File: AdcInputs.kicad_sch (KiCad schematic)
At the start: 38 parts, among them U31 AMC1100DWV, U32 AMC1100DWV, U33 AMC1100DWV, U34 AMC1100DWV, U6 CD4051B, U7 CD4051B, U8 CD4052B, U9 LTV-247

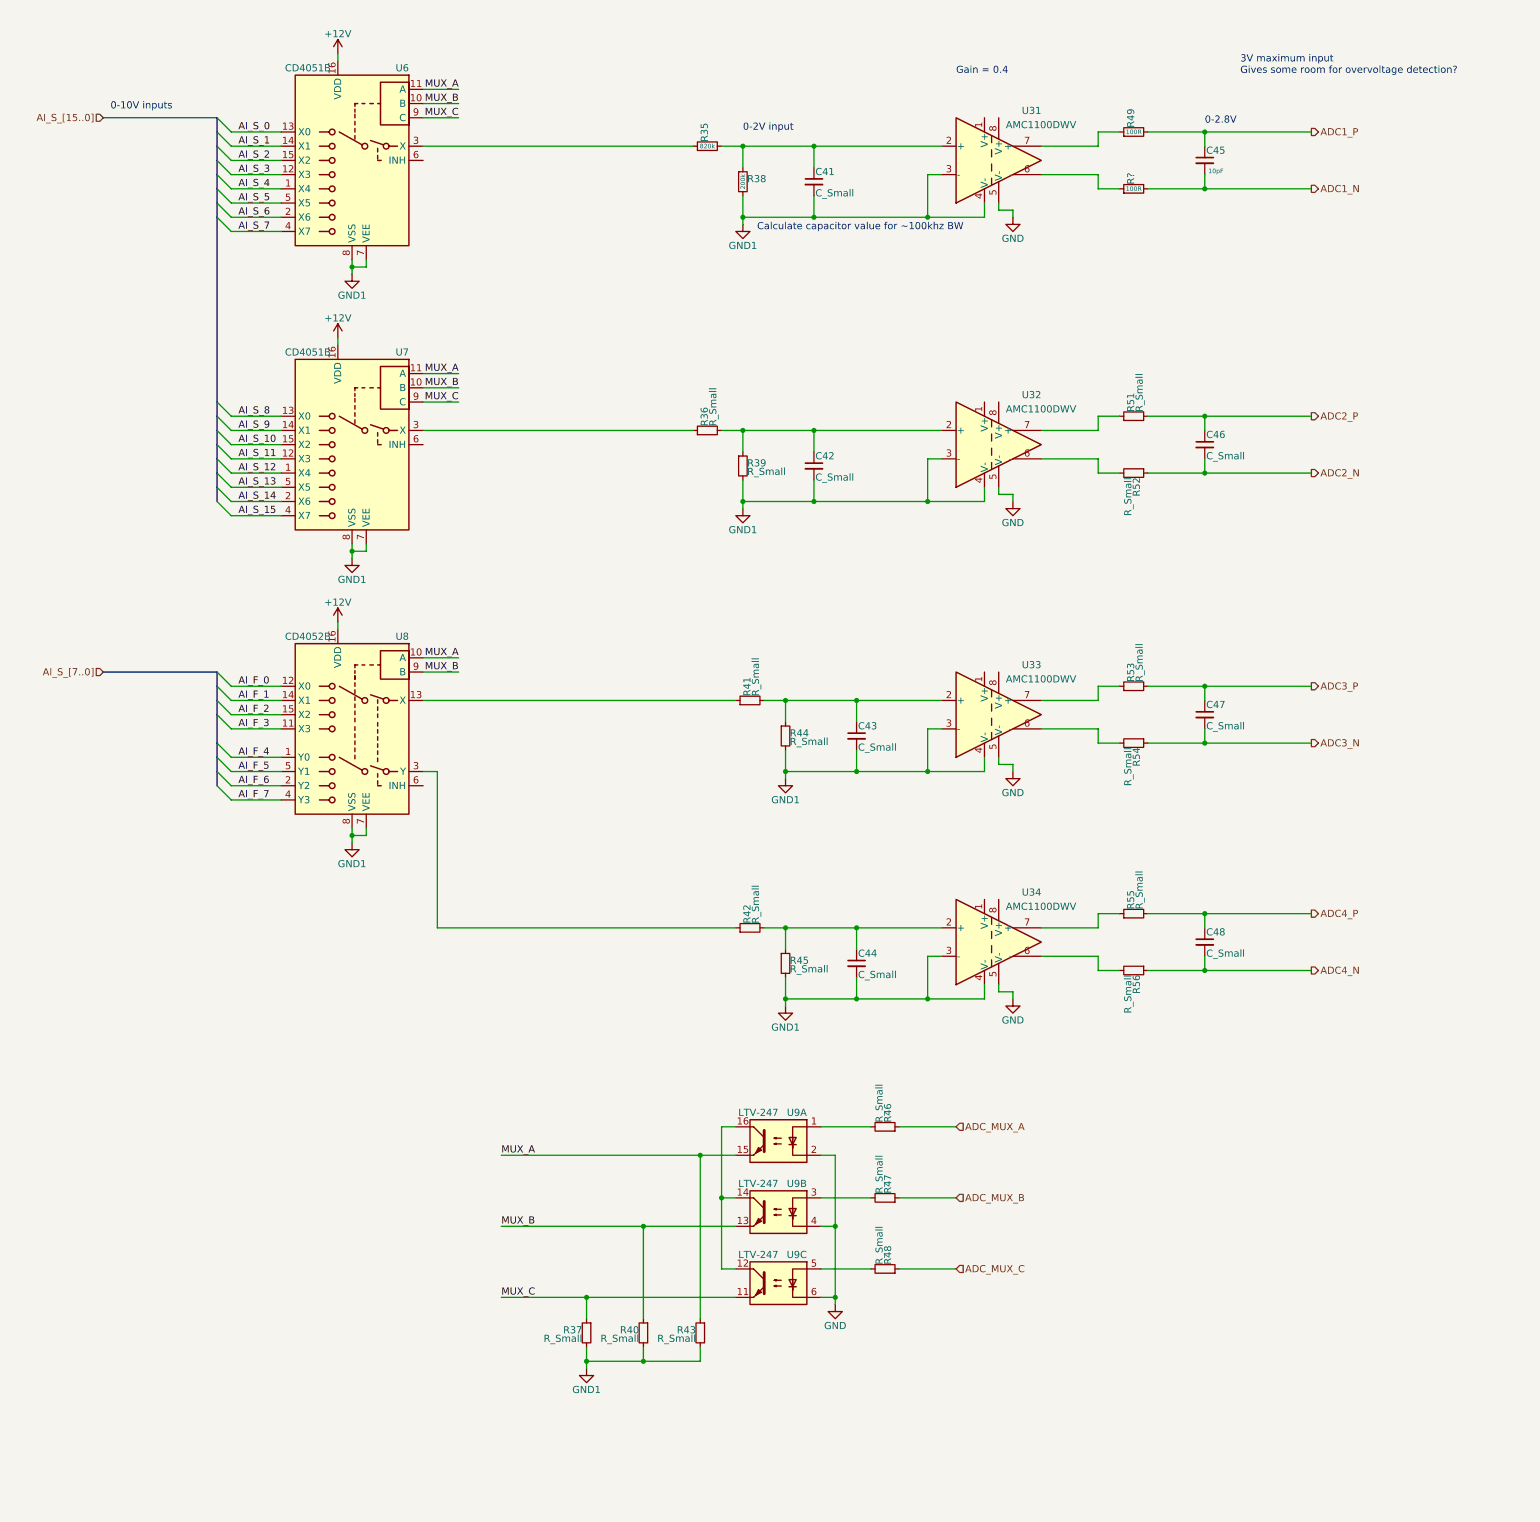
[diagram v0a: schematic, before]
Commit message: analog inputs, timer IO
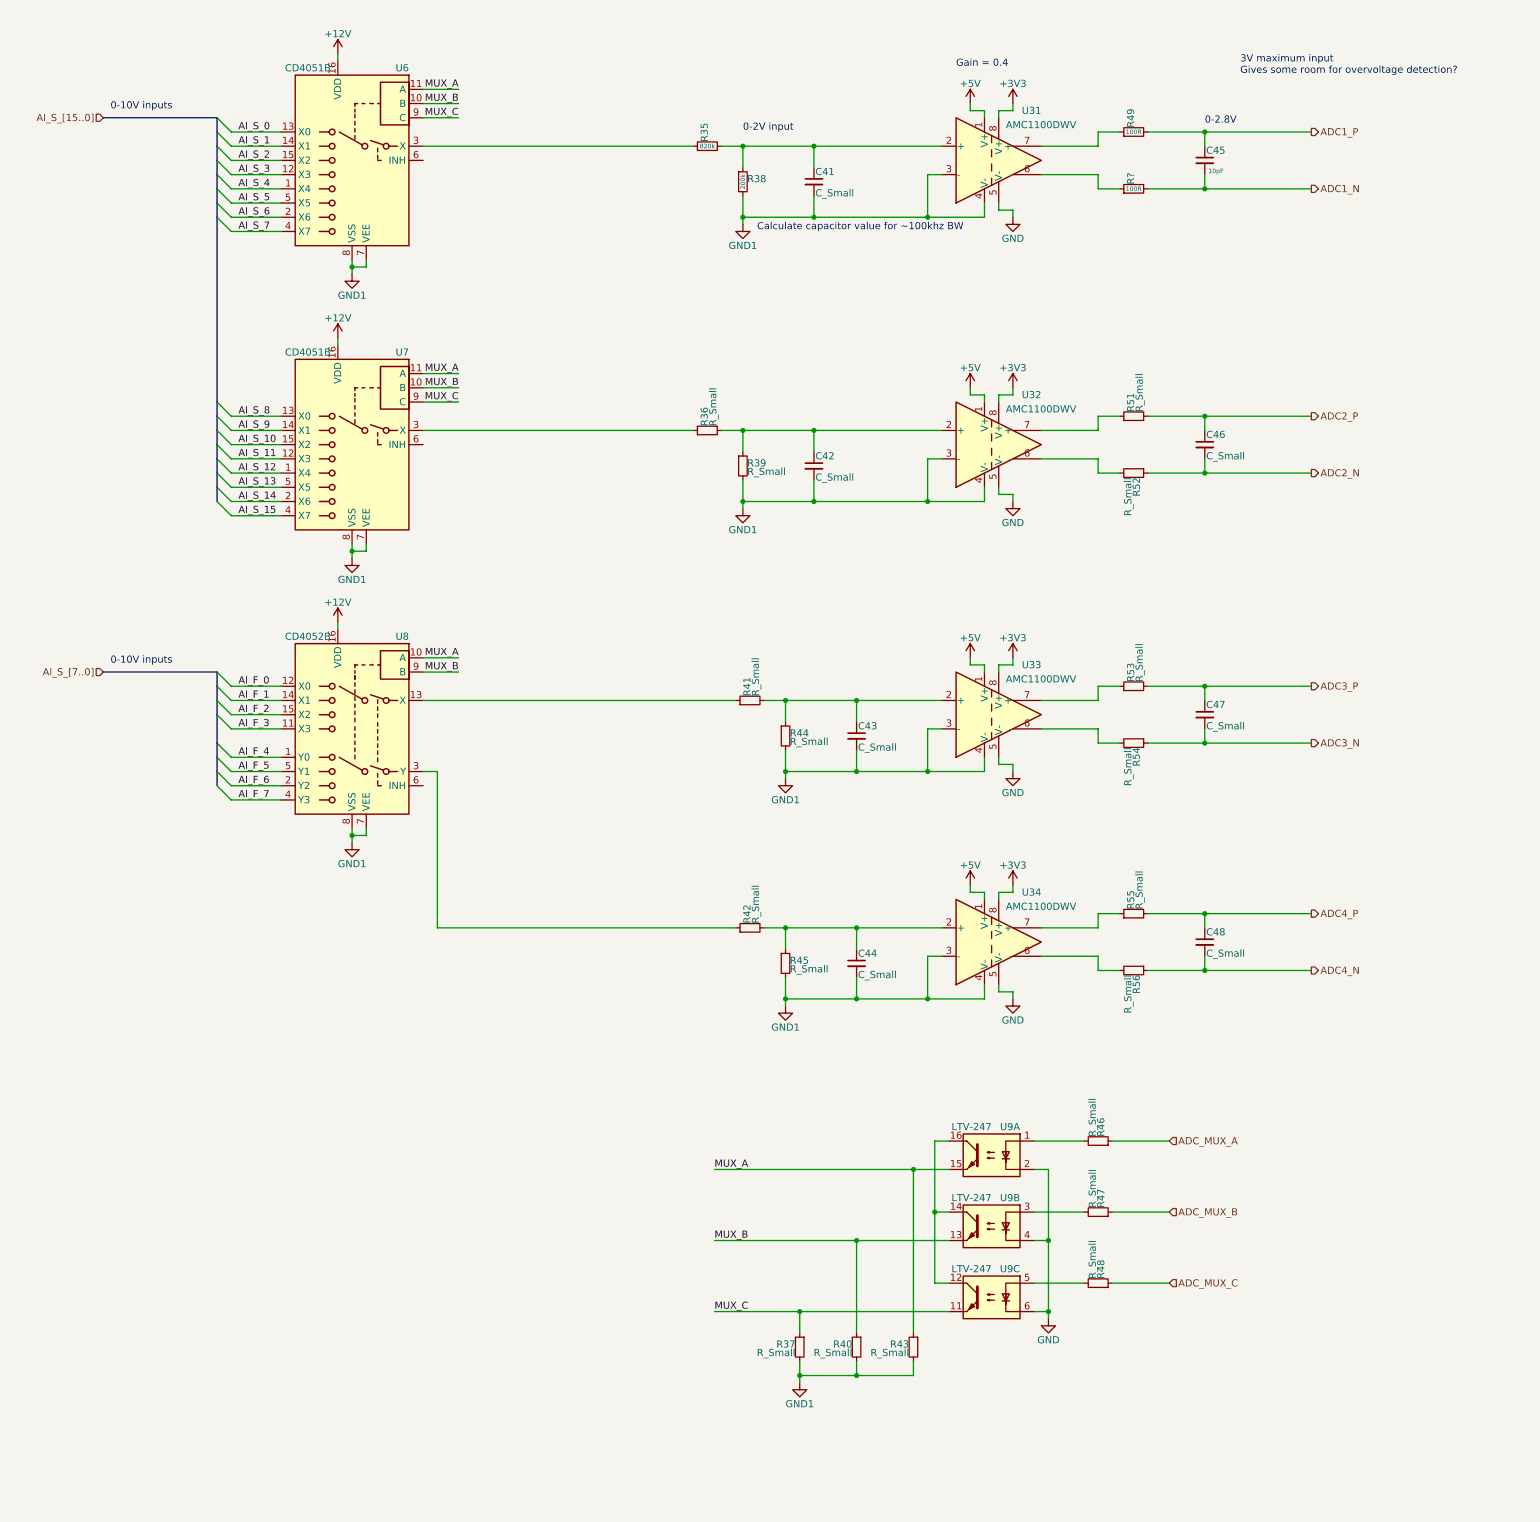
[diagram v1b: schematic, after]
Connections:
- net +5V: now reaches U31.1 (V+)
- net +5V: now also U32.1 (V+), U33.1 (V+), U34.1 (V+)
- net +3V3: now reaches U31.8 (V+)
- net +3V3: now also U32.8 (V+), U33.8 (V+), U34.8 (V+)
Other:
- moved on the sheet: R37, R40, R43, R46, R47, R48, U9A, U9B, U9C

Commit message: first draft schematic?
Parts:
- added C51, C52, C53, C54, C55, C56, C57, C58: C_Small, Capacitor_SMD:C_0603_1608Metric, symbol Device:C_Small
- C41, C42, C43, C44, C46, C47, C48: footprint (none) -> Capacitor_SMD:C_0603_1608Metric
- R36, R37, R39, R40, R41, R42, R43, R44, R45, R46, R47, R48, R51, R52, R53, R54, R55, R56: footprint (none) -> Resistor_SMD:R_0603_1608Metric
- gave numbers to parts that had none: 1
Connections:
- net ADC1_N: now also C52.1
- net ADC1_P: now also C51.2
- net ADC2_N: now also C54.1
- net ADC2_P: now also C53.2
- net ADC3_N: now also C56.1
- net ADC3_P: now also C55.2
- net ADC4_N: now also C58.1
- net ADC4_P: now also C57.2
- net GND: now also C51.1, C52.2, C53.1, C54.2, C55.1, C56.2, C57.1, C58.2
